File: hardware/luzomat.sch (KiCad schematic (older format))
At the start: 58 parts, among them J3 40HAT, J9 CONN_01X02, U2 CAT24C32

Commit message: layout first draft
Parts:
- removed J9: CONN_01X02, Connector_PinHeader_2.54mm:PinHeader_1x02_P2.54mm_Vertical, symbol Connector_Generic:Conn_01x02
- removed J?: Screw_Terminal_01x04, symbol Connector:Screw_Terminal_01x04
- removed R29: 10K, Resistor_SMD:R_0603_1608Metric_Pad0.84x1.00mm_HandSolder, symbol Device:R
- removed R6, R8: 3.9K, Resistor_SMD:R_0603_1608Metric_Pad0.84x1.00mm_HandSolder, symbol Device:R
- removed R?: 270R, symbol Device:R
- removed R? (x2): 10k, symbol Device:R
- removed U2: CAT24C32, Package_SOIC:SOIC-8_3.9x4.9mm_P1.27mm, symbol luzomat-rescue:CAT24C32-raspberrypi_hat
- added C11, C12, C14, C15, C18, C19, C20, C21, C22, C5, C8: 100n, Capacitor_SMD:C_0805_2012Metric_Pad1.15x1.40mm_HandSolder, symbol Device:C
- added C4, C6, C7, C9: 10n, Capacitor_SMD:C_0805_2012Metric_Pad1.15x1.40mm_HandSolder, symbol Device:C
- added H9: 3mm_Mounting_Hole, project_footprints:NPTH_3mm_ID, symbol luzomat-rescue:Mounting_Hole-Mechanical
- added J17, J18, J5, J6: Screw_Terminal_01x02, TerminalBlock:TerminalBlock_bornier-2_P5.08mm, symbol Connector:Screw_Terminal_01x02
- added L1, L2: 600R@100MHz, Inductor_SMD:L_0805_2012Metric_Pad1.15x1.40mm_HandSolder, symbol Device:L_Core_Ferrite
- added R1, R2: 3k9, Resistor_SMD:R_0805_2012Metric_Pad1.15x1.40mm_HandSolder, symbol Device:R
- added R10, R11, R12, R13, R14, R9: 2k2, Resistor_SMD:R_0805_2012Metric_Pad1.15x1.40mm_HandSolder, symbol Device:R
- added R16, R17, R19, R20, R21, R22: 100R, Resistor_SMD:R_0805_2012Metric_Pad1.15x1.40mm_HandSolder, symbol Device:R
- added R23: 270R, Resistor_SMD:R_0805_2012Metric_Pad1.15x1.40mm_HandSolder, symbol Device:R
- added R26, R27, R3: 10k, Resistor_SMD:R_0805_2012Metric_Pad1.15x1.40mm_HandSolder, symbol Device:R
- added R40: n/a, Resistor_SMD:R_0805_2012Metric_Pad1.15x1.40mm_HandSolder, symbol Device:R
- added U1: CAT24C256, Package_SO:SOIC-8_3.9x4.9mm_P1.27mm, symbol Memory_EEPROM:CAT24C256
- added U3, U4: MAX31856, Package_SO:TSSOP-14_4.4x5mm_P0.65mm, symbol Sensor_Temperature:MAX31856
- C1, C10, C13, C16, C17, C2, C3: renamed from C?; footprint (none) -> Capacitor_SMD:C_0805_2012Metric_Pad1.15x1.40mm_HandSolder
- F1, F2: renamed from F?; footprint (none) -> Fuse:Fuseholder_Cylinder-5x20mm_Bulgin_FX0457_Horizontal_Closed
- J1, J10, J11, J12, J13, J14, J15, J16, J19, J2, J20, J21, J7, J8, J9: renamed from J?; footprint (none) -> TerminalBlock:TerminalBlock_bornier-2_P5.08mm
- Q1, Q3: renamed from Q?; symbol dk_Transistors-FETs-MOSFETs-Single:DMG2305UX-13 -> luzomat-rescue:DMG2305UX-13-dk_Transistors-FETs-MOSFETs-Single
- R15, R18, R24, R25, R4, R5, R6, R7, R8: renamed from R?; footprint (none) -> Resistor_SMD:R_0805_2012Metric_Pad1.15x1.40mm_HandSolder
- U2: renamed from U?; footprint (none) -> Package_TO_SOT_THT:TO-220-3_Horizontal_TabDown
- U5: renamed from U?; symbol dk_Logic-Multivibrators:SN74LVC1G123DCTR -> luzomat-rescue:SN74LVC1G123DCTR-dk_Logic-Multivibrators
- gave numbers to parts that had none: 7
- renumbered H2 to H3, H3 to H5, H4 to H7
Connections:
- net labels added: miso, mosi, sck, ~cs1, ~cs2
- wire segments 85 -> 154
- no-connect marks 0 -> 4
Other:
- note added: "3/4: led"
- note added: "led"
- note added: "photomos"
- moved on the sheet: C10, C13, C16, C17, H1, H2, H3, H4, H5, H6, H7, H8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

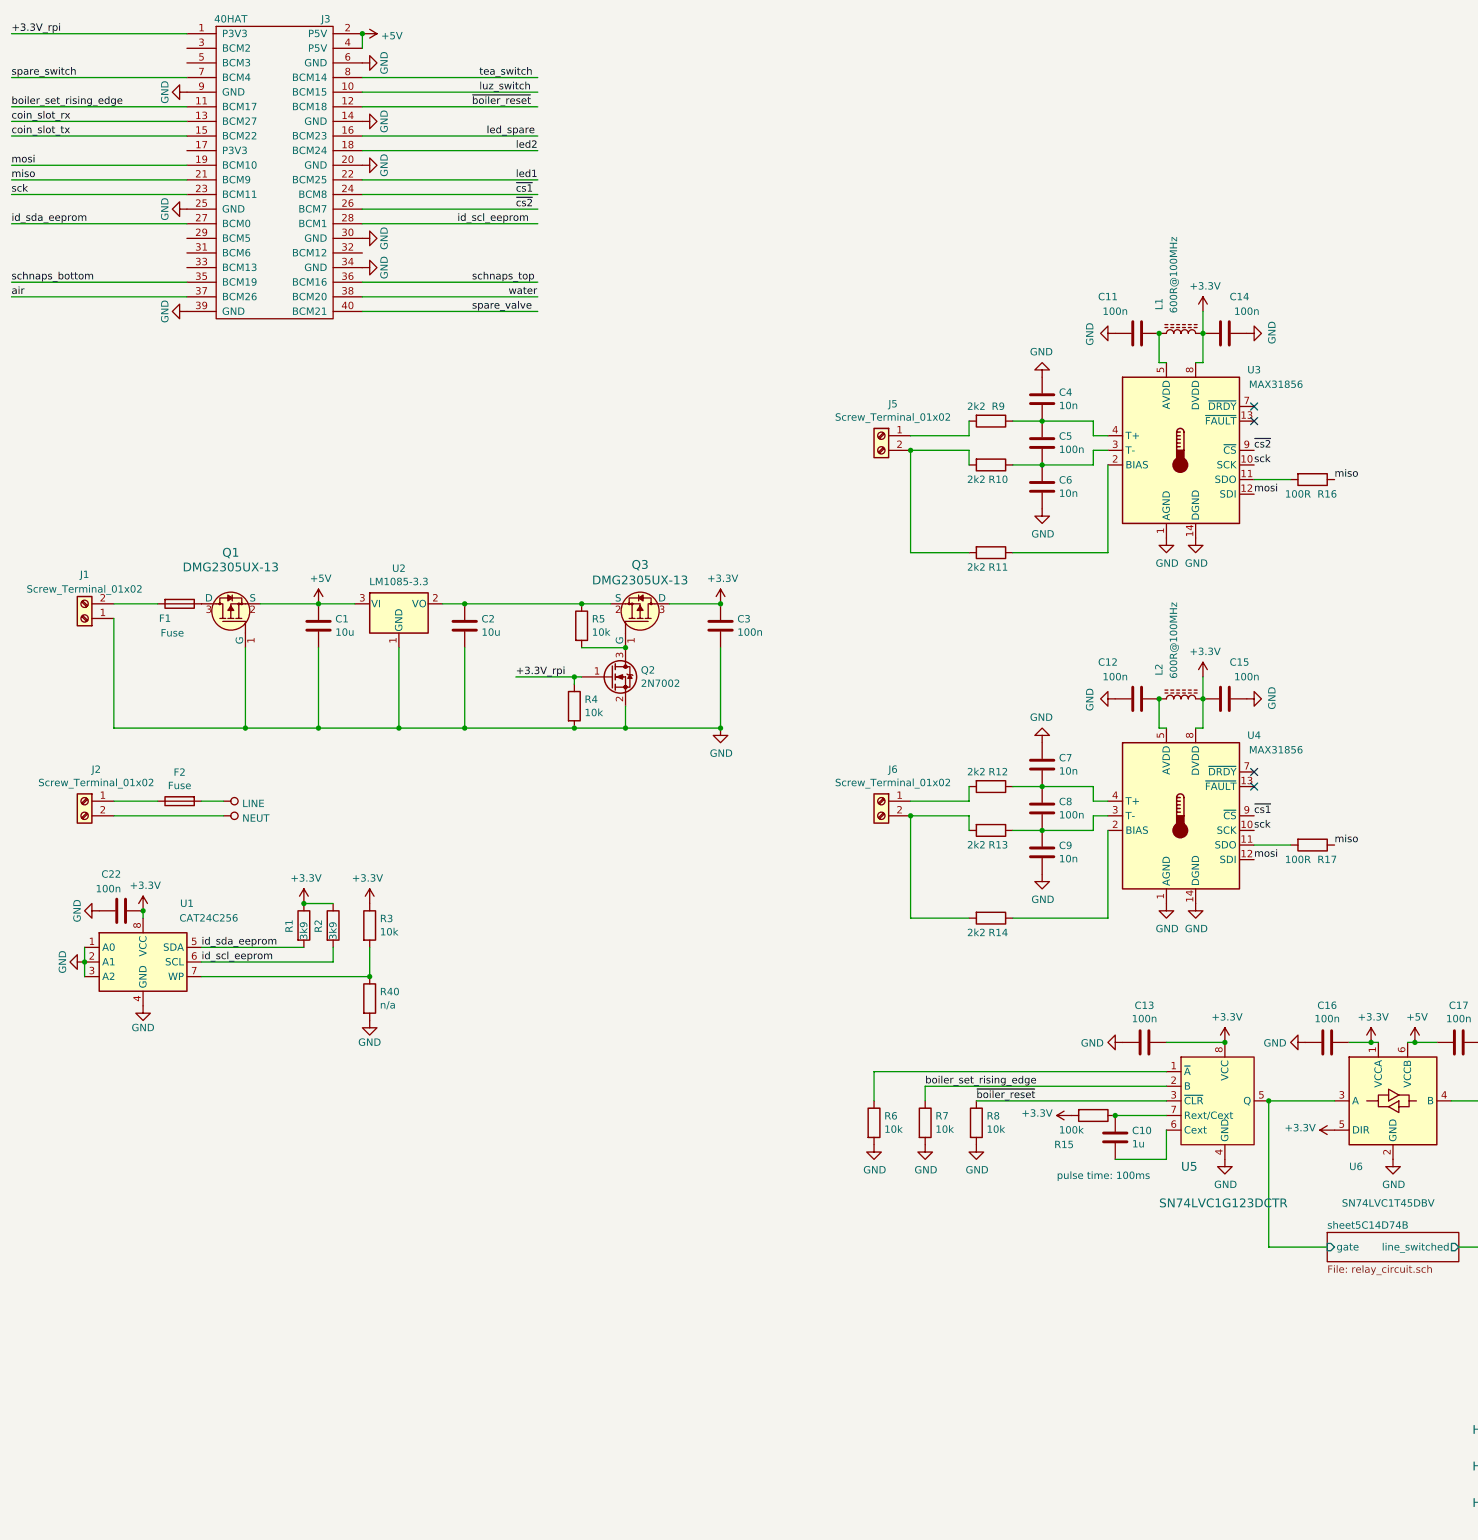
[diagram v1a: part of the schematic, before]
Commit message: added testpoints and silkscreen
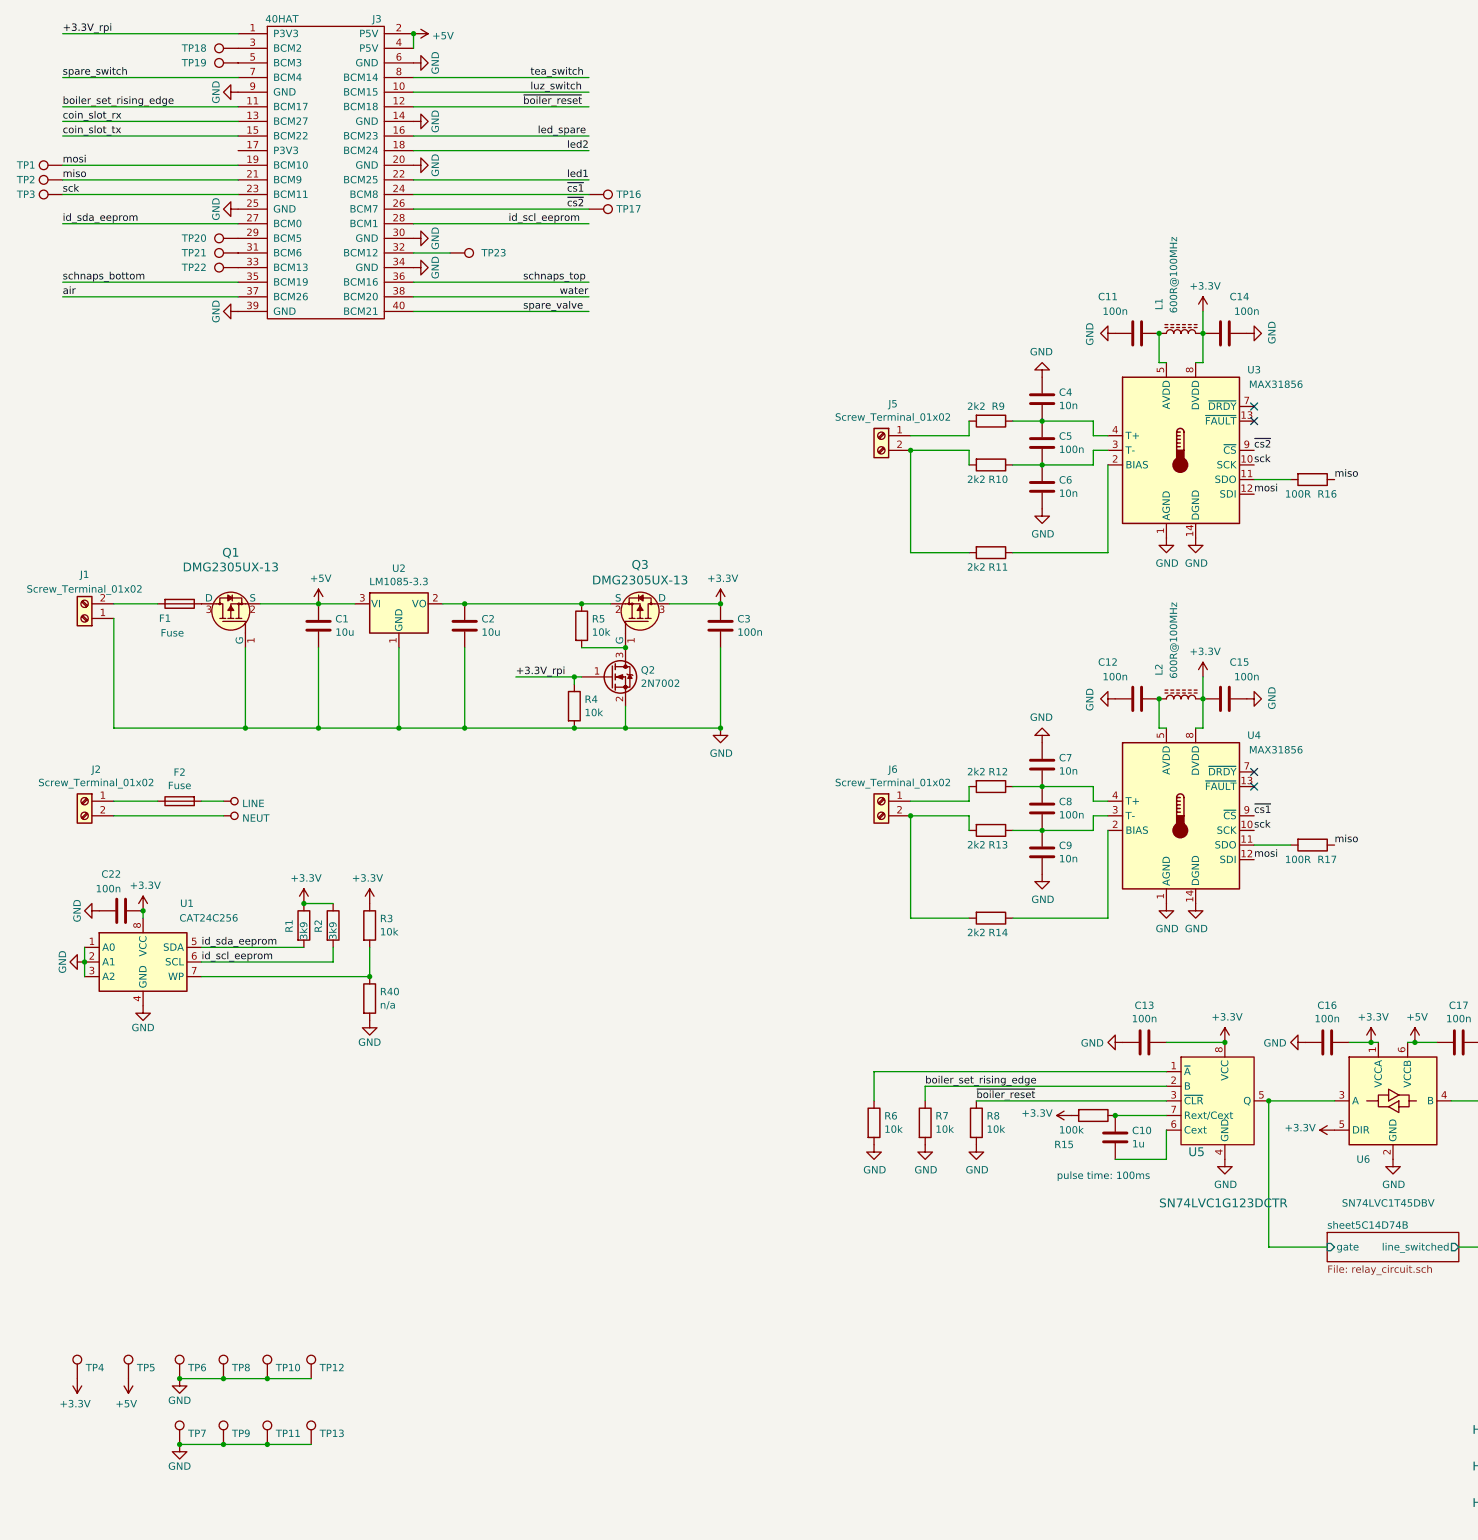
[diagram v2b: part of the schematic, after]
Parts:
- added TP1, TP10, TP11, TP12, TP13, TP16, TP17, TP18, TP19, TP2, TP20, TP21, TP22, TP23, TP3, TP4, TP5, TP6, TP7, TP8, TP9: TestPoint, TestPoint:TestPoint_THTPad_D2.5mm_Drill1.2mm, symbol Connector:TestPoint
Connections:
- wire segments 154 -> 161
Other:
- moved on the sheet: J3
